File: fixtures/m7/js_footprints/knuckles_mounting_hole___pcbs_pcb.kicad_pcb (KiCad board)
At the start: 2 copper layers, 1 part

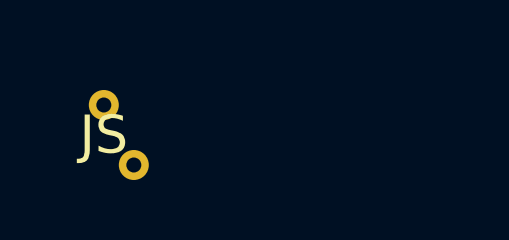
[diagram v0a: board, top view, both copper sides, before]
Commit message: Add knuckles JS fixture and upstream parity test
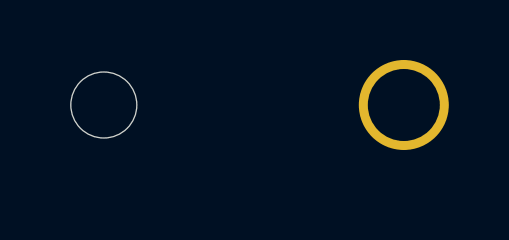
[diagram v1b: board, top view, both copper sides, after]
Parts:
- removed FP1: , js_simple
- added MH1: , ceoloide:mounting_hole_npth, F.Cu at (0.00, 0.00)
- added MH2: , ceoloide:mounting_hole_npth, B.Cu at (10.0, 0.00)
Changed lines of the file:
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@@
   )
   (net 0 "")
-(net 1 "GND")
-(net 2 "FP1_A")
-(footprint "js_simple"
-  (layer F.Cu)
-  (at 0 0 0)
-  (property "Reference" "FP1" (at 0 0) (layer F.SilkS) hide)
-  (pad "1" thru_hole circle (at 0 0) (size 1 1) (drill 0.5) (layers *.Cu *.Mask) (net 1 "GND"))
-  (pad "2" thru_hole circle (at 1 2) (size 1 1) (drill 0.5) (layers *.Cu *.Mask) (net 2 "FP1_A"))
-  (fp_text user "JS" (at 0 1) (layer F.SilkS))
+  (footprint "ceoloide:mounting_hole_npth"
+    (layer "F.Cu")
+    (at 0 0 0)
+    (property "Reference" "MH1"
+      (at 0 2.55 0)
+      (layer "F.SilkS")
+      hide
+      (effects (font (size 1 1) (thickness 0.15)))
+    )
+    (pad "" np_thru_hole circle
+      (at 0 0 0)
+      (size 2.2 2.2)
+      (drill 2.2)
+      (layers "*.Cu" "*.Mask")
+    )
+  )
+  (footprint "ceoloide:mounting_hole_npth"
+    (layer "B.Cu")
+    (at 10 0 0)
+    (property "Reference" "MH2"
+      (at 0 2.55 0)
+      (layer "B.SilkS")
+      hide
+      (effects (font (size 1 1) (thickness 0.15)))
+    )
+    (pad "" np_thru_hole circle
+      (at 0 0 0)
+      (size 3.0 3.0)
+      (drill 2.4)
+      (layers "*.Cu" "*.Mask")
+    )
+  )
 )
-)
